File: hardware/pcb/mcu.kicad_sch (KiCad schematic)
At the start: 13 parts, among them SW1 RESET, SW2 BOOT, U6 ESP32-C6

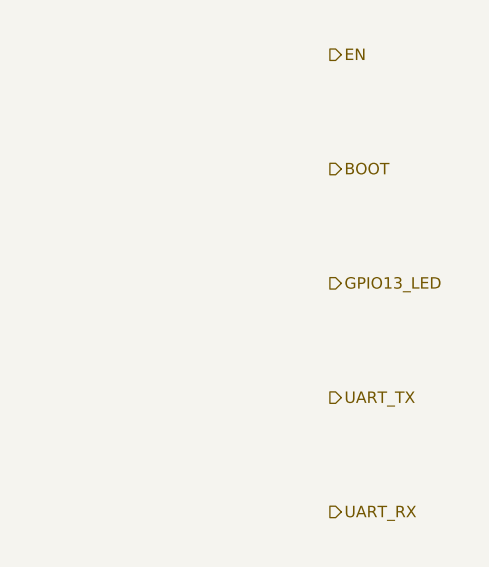
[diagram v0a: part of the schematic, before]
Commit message: hw(pcb): electrical review pass — fix 3V3 regulator variant, boost topology, GPIO13 LED conflict
Full electrical-correctness-gate review of the fresh-start design. Two of
the four CRITICALs from the 2026-05-25 senior review were resolved
incorrectly; this pass corrects them and fixes new findings:

- U1: AP63205WU is the 5 V fixed variant and the R_FBH/R_FBL values
  (560k/124k) assume a 0.6 V reference no AP6320x has — every
  combination overdrives the 3V3 rail. Swap to AP63203WU (3.3 V fixed),
  FB tied to +3V3, R_FBH/R_FBL marked DNP.
- MT3608B VLOOP: documented wiring was a buck topology and the BOM had
  no output rectifier (async boost cannot work without one). Corrected
  to VBAT→L1→SW, added D15 (SS34) and a Q3/Q4 load-disconnect so VBAT
  doesn't leak to the loop terminals through L1+D15 during deep sleep.
- Status LED moved GPIO13 → GPIO14: a green LED + 1k on GPIO13 holds
  the factory-reset strap LOW at boot → NVS wipe every boot. TP13 pad
  added for field factory reset.
- Battery divider reworked to high-side P-FET (Q5): the low-side switch
  left AIN2 biased above ADS1115 VDD through R7 (~14 uA sleep leak).
  C8 100nF → 1nF to fit the firmware's 1 ms enable window.
- TVS D8/D14 SMAJ28CA → SMAJ24CA (zero margin to CN3722 28 V abs max);
  C17 → 35 V/1206; C21 → 50 V; D6 footprint SOD-123 → SMB.
- /CHRG_SOLAR pull-up (R25), VBOOST_EN pull-down (R27), ESP32 EN RC
  (R15/C36) added; C25 duplicate bootstrap cap deleted; C16 assigned as
  U1 VIN bulk.
- schematic_connections.md rewritten pin-name-based with a symbol
  pin-number verification table and datasheet-verification blocker list;
  BOM/placement/guide/placement-script reconciled (phantom refdes,
  wrong ADS1115 pin numbers, mis-documented MPPT divider, shunt return
  path contradiction).

Flagged, not fixed: TP5100 cannot charge 2S from 5 V USB (step-down
charger) — needs an IC swap; schematic still has zero drawn wires; five
IC symbol pinouts pending datasheet verification before ordering.

Co-Auth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
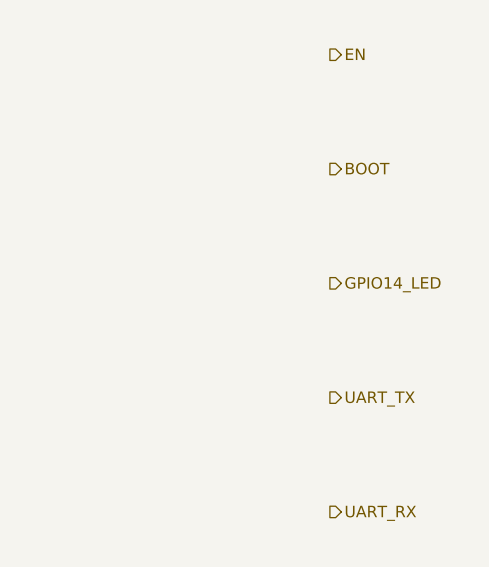
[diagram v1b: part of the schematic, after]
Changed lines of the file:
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@@
 		)
 	)
-	(hierarchical_label "GPIO13_LED"
+	(hierarchical_label "GPIO14_LED"
 		(shape output)
 		(at 254 88.9 0)

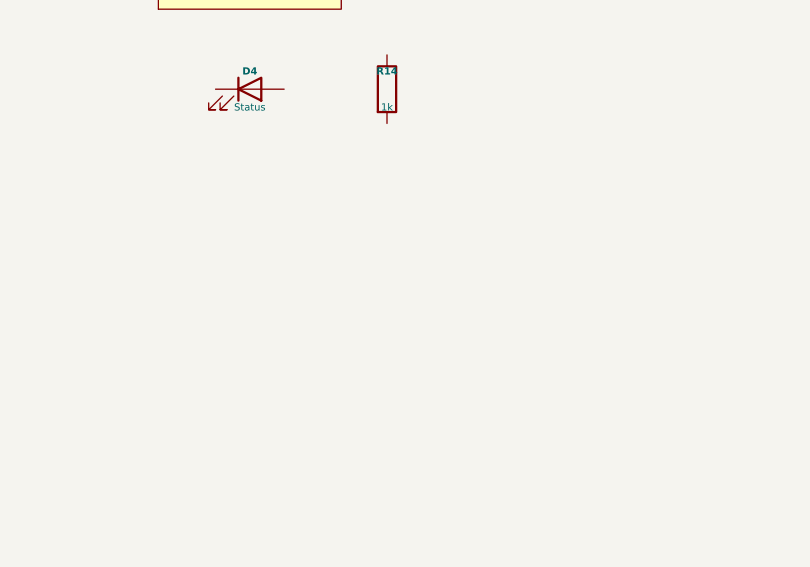
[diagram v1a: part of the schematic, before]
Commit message: hw(pcb): symbol pass — all parts placed, CN3722 redrawn TSSOP-16, CV/MPPT reference bug fixed
Clears the layout gate from senior_review_2026-07-06.md (CRITICALs 1-3)
and fixes a newly found CRITICAL:

- CN3722 CV divider was computed with the CN3791's 1.205 V reference;
  the CN3722's FB reference is 2.416 V (datasheet Rev 1.1, p.4), so the
  documented 590k/100k divider would regulate the 2S pack at ~16.7 V.
  R33 590k -> 243k (8.287 V; formula V_REG = 2.416 x (1 + Rh/Rl) stated
  at every location). Same root cause in the MPPT divider: ref is
  1.04 V, not 1.205 V — old values set the tracking point at 4.8 V,
  below the chip's 7.5 V minimum VCC; R20 36k -> 158k (V_MP ~17.5 V for
  a 12 V-nominal panel, flagged for recompute against the real panel).
- CN3722 symbol redrawn as the real TSSOP-16 (was an 8-pin fiction with
  a nonexistent VPROG pin); full external buck stage placed: M_SOLAR
  P-FET, D16 series + D_SOLAR catch Schottkys, L_SOLAR 47uH, R19
  repurposed as the 0.4R CSP-BAT sense resistor (500 mA), VG cap,
  COM1/2/3 compensation network, RT_SOLAR 10k NTC on TEMP (solar-path
  cold-charge cutoff — review finding O-1 closed for both chargers).
- IP2326 drawn as the verified 24-pin+EPAD part replacing TP5100
  (R36/R37 instances deleted), with R_VSET 120k, RISET 90k, L3 2.2uH,
  RT1 NTC, BST/VSYS caps. Footprint welld:IP2326_TBD pending the LCSC
  package code.
- MT3608B symbol numbering fixed to the standard family map
  (SW=1/GND=2/FB=3/EN=4/IN=5/NC=6; bench-verify note added — datasheet
  fetch was proxy-blocked).
- All previously missing symbols placed: D15, Q3/R29, Q4/R27, Q5/R16,
  R25 (power); R15/C36 EN RC, TP13 (mcu). Values synced: D8/D14
  SMAJ24CA, C8 1nF, C17 35V/1206, F2 2A-hold PTC.
- schematic_connections.md resolution/blocker tables updated; sheets
  still have no drawn wires — the doc remains the wiring authority
  until the wiring pass.

Co-Authored-By: Claude Fable 5 <noreply@anthropic.com>
Claude-Session: https://claude.ai/code/session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
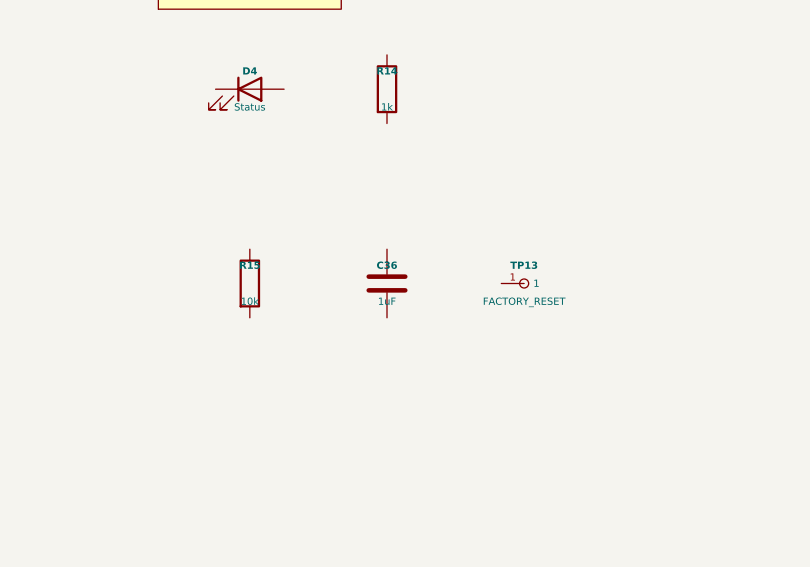
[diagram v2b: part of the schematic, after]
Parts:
- added C36: 1uF, Capacitor_SMD:C_0402_1005Metric, symbol Device:C
- added R15: 10k, Resistor_SMD:R_0402_1005Metric, symbol Device:R
- added TP13: FACTORY_RESET, TestPoint:TestPoint_Pad_1.0x1.0mm, symbol welld:TestPoint_Pad

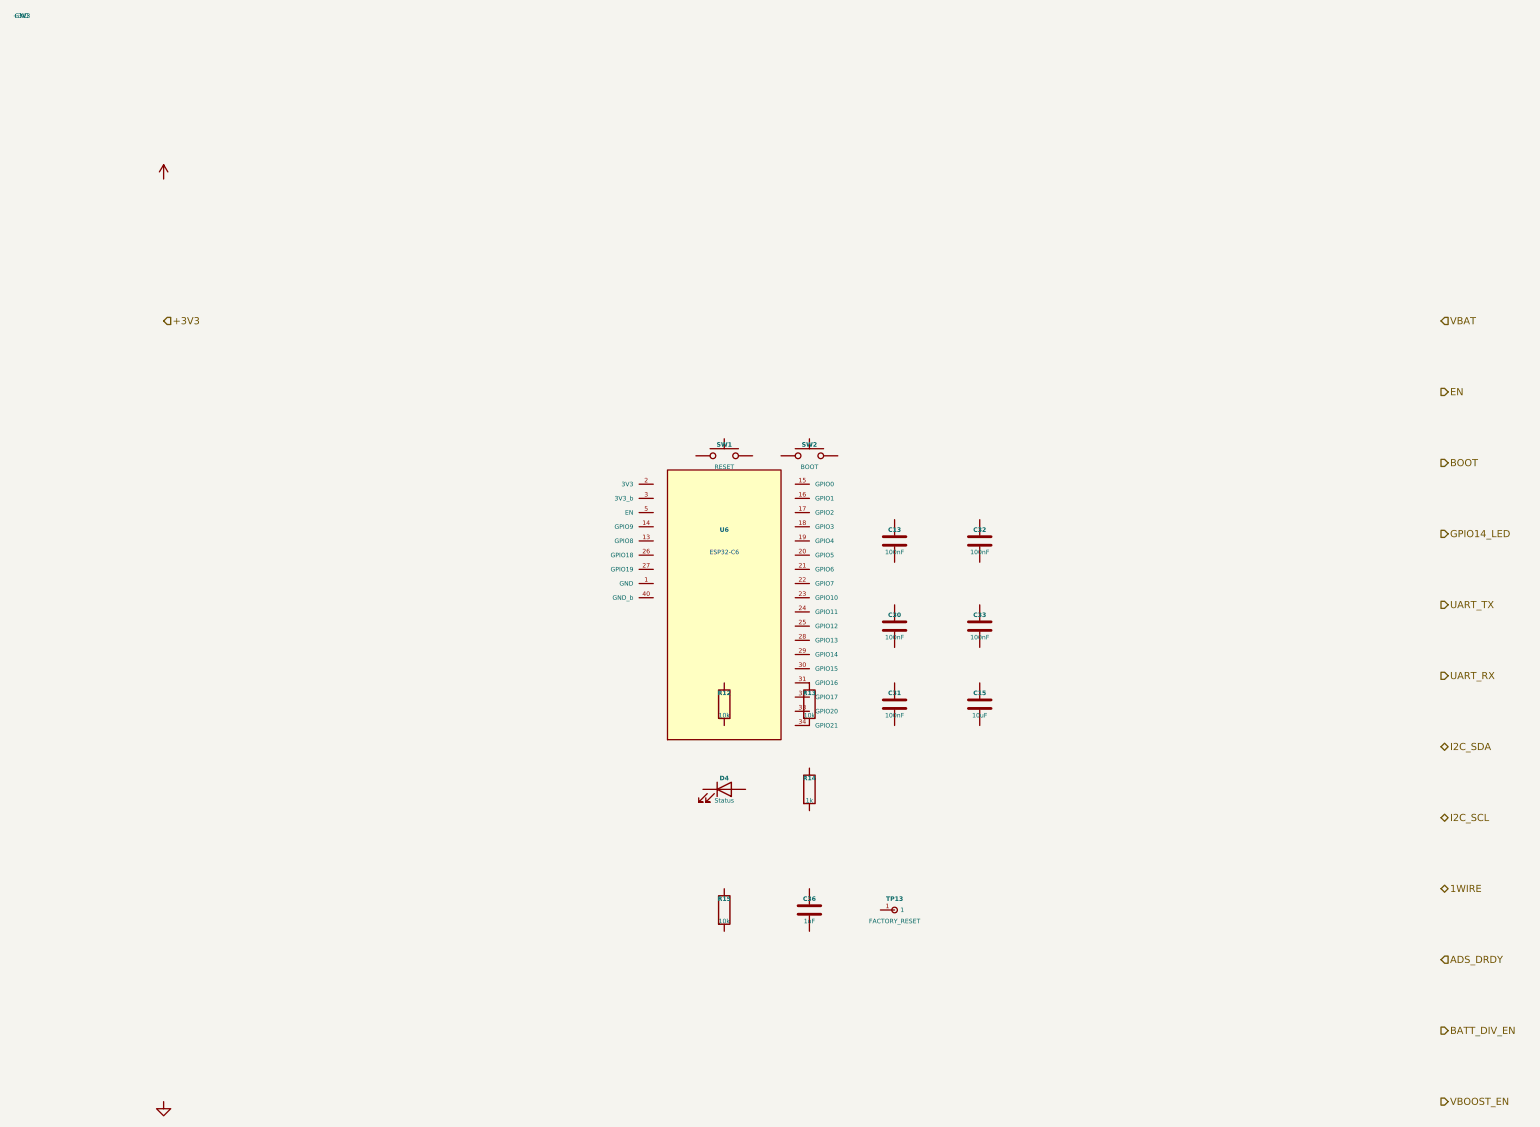
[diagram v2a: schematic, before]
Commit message: hw(pcb): wiring pass — schematic fully wired, netlist machine-verified (0 mismatches)
All four sheets wired with stub+label connectivity (434 wires, 21
explicit no-connects, PWR_FLAGs on undriven rails): power rails on
global labels, cross-sheet signals on hierarchical labels + rebuilt
top-sheet pins (24 hierarchical nets; vestigial ADC_CH* pins deleted,
GPIO14_LED corrected to the mcu-local net it really is), sheet-local
nets on local labels.

Verification (kicad-cli for the KiCad-10 format is not installable
here): hardware/pcb/kicad_wire_script.py generates the connectivity
from an embedded intent table derived from schematic_connections.md;
hardware/pcb/netlist_check.py independently re-extracts pin->net
geometrically (union-find over wires/labels/sheet pins) and diffs —
395 pins, 77 nets, 0 mismatches (output committed). Native KiCad 10
ERC + resave queued for the first interactive open.

Notable resolutions (recorded as design change #17): AP63203 FB tied
to +3V3 with the DNP divider floated at its midpoint; MT3608B pin 6
etype relaxed to passive so C_BST wiring is ERC-legal; IP2326 DM/DP
floated with no-connects (adapter detection is a two-wire future
change); D11 oriented cathode-to-VLOOP; decorative corner power
symbols replaced with real rail connectivity.

placement_constraints.md: Group G rewritten for the IP2326 hot loop,
new Group L for the CN3722 external buck (Kelvin CSP/BAT pair).
Top remaining risk flagged in blockers: AP63203 BST is NC per the
wiring doc but the AP6320x family likely requires a BST-SW cap —
resolve before layout freeze.

Co-Authored-By: Claude Fable 5 <noreply@anthropic.com>
Claude-Session: https://claude.ai/code/session_01VtMFY5Q94iYbsNPpLcPJyK
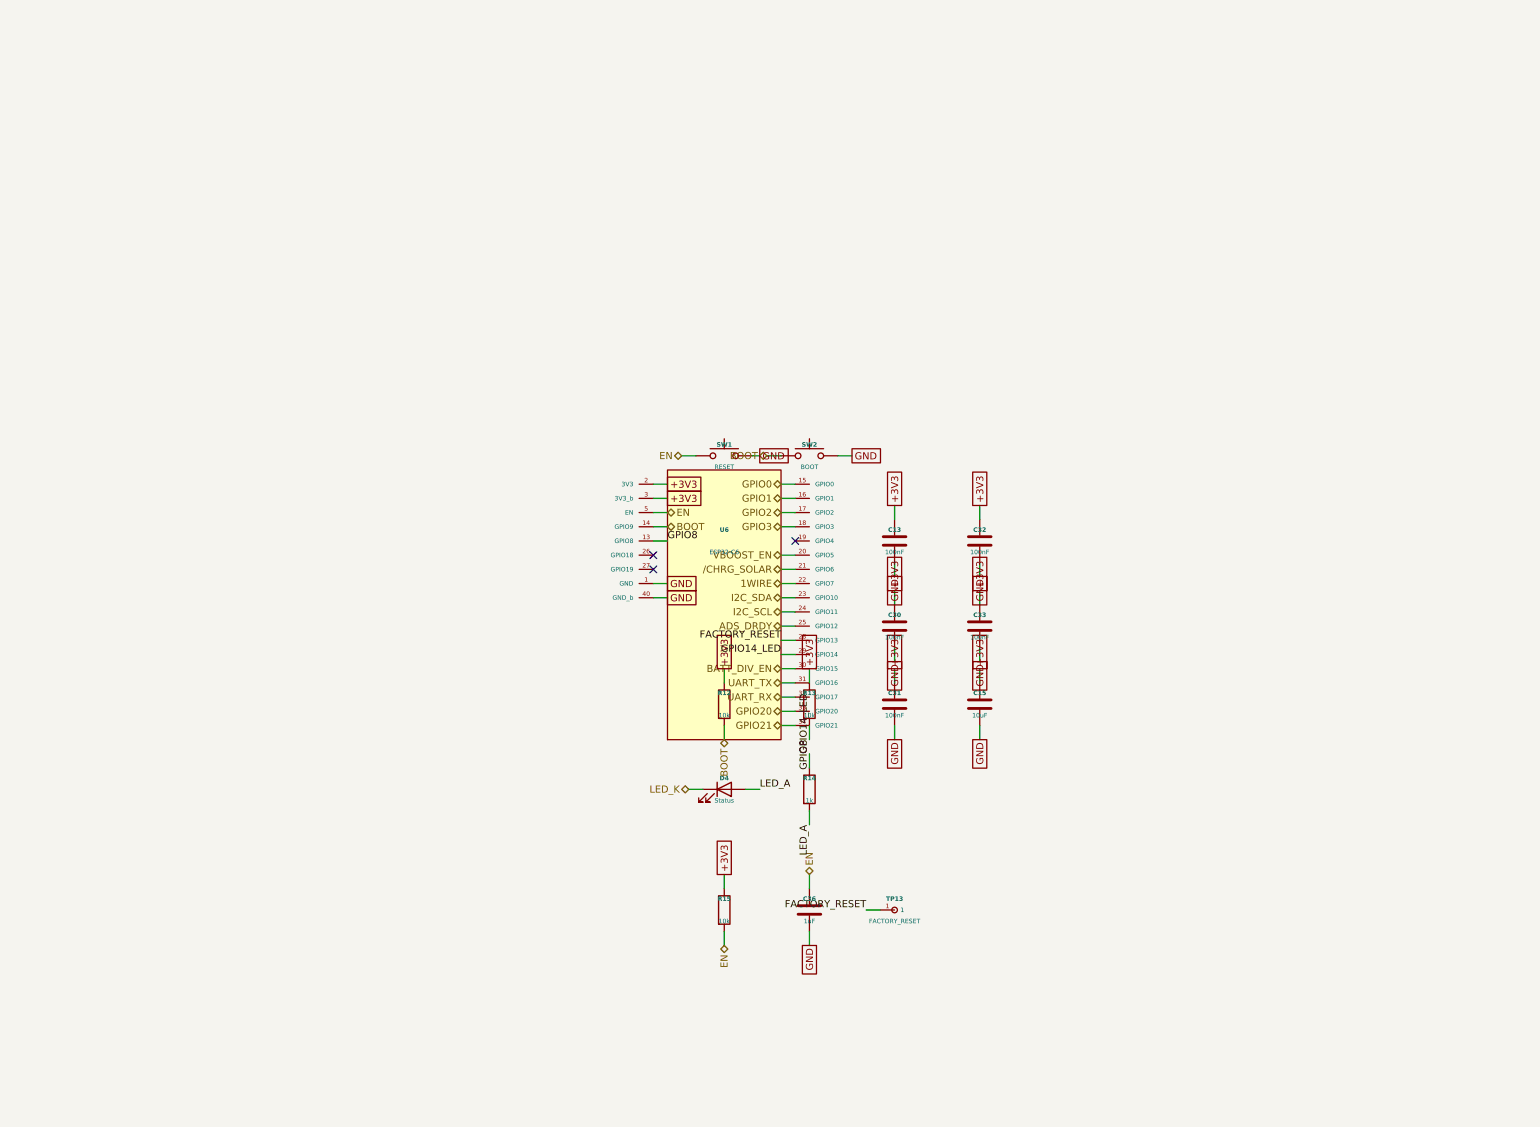
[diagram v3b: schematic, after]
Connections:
- net +3V3: now also C13.1, C15.1, C30.1, C31.1, C32.1, C33.1, R12.1, R13.1, R15.1, U6.2 (3V3), U6.3 (3V3_b)
- net 1WIRE: now also U6.22 (GPIO7)
- net ADS_DRDY: now also U6.25 (GPIO12)
- net BATT_DIV_EN: now also U6.30 (GPIO15)
- net BOOT: now also R12.2, SW2.1, U6.14 (GPIO9)
- net EN: now also C36.1, R15.2, SW1.1, U6.5 (EN)
- net GND: now also C13.2, C15.2, C30.2, C31.2, C32.2, C33.2, C36.2, SW1.2, SW2.2, U6.1 (GND), U6.40 (GND_b)
- net GPIO14_LED: now also R14.1, U6.29 (GPIO14)
- net I2C_SCL: now also U6.24 (GPIO11)
- net I2C_SDA: now also U6.23 (GPIO10)
- net UART_RX: now also U6.32 (GPIO17)
- net UART_TX: now also U6.31 (GPIO16)
- net VBOOST_EN: now also U6.20 (GPIO5)
- net LED_A: now reaches R14.2
- net LED_A: now also D4.2 (A)
- net LED_K: now reaches D4.1 (K)
- net FACTORY_RESET: now reaches TP13.1
- net FACTORY_RESET: now also U6.28 (GPIO13)
- net GPIO8: now reaches U6.13 (GPIO8)
- net GPIO8: now also R13.2
- net GPIO0: now reaches U6.15 (GPIO0)
- net GPIO1: now reaches U6.16 (GPIO1)
- net GPIO2: now reaches U6.17 (GPIO2)
- net GPIO3: now reaches U6.18 (GPIO3)
- net /CHRG_SOLAR: now reaches U6.21 (GPIO6)
- net GPIO20: now reaches U6.33 (GPIO20)
- net GPIO21: now reaches U6.34 (GPIO21)
- no-connect marks 0 -> 3
